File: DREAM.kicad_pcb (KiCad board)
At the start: 2 copper layers, 100 x 60 mm, 137 parts, among them J401 KLDX-0202-B, J402 EBWA-02-B, J501 Conn_ST_STDC14, J502 USB4105-GF-A, J601 1-1337535-0, J602 1-1337535-0, J603 1-1337535-0, J701 PH1-02-UA, Q401 MCU18P10Y-TP, SW501 PTS526SK15SMTR2 LFS, U401 TPS7A2030PDBVR, U501 STM32G441KBT6, U502 USBLC6-2SC6, U601 TSV912AIDR, U602 TSV912AIDR, U603 LM358LVIDR, U604 TSV912AIDR, U605 TSV912AIDR, U701 LM358LVIDR, U702 LM358LVIDR, Y501 ATS08A-E

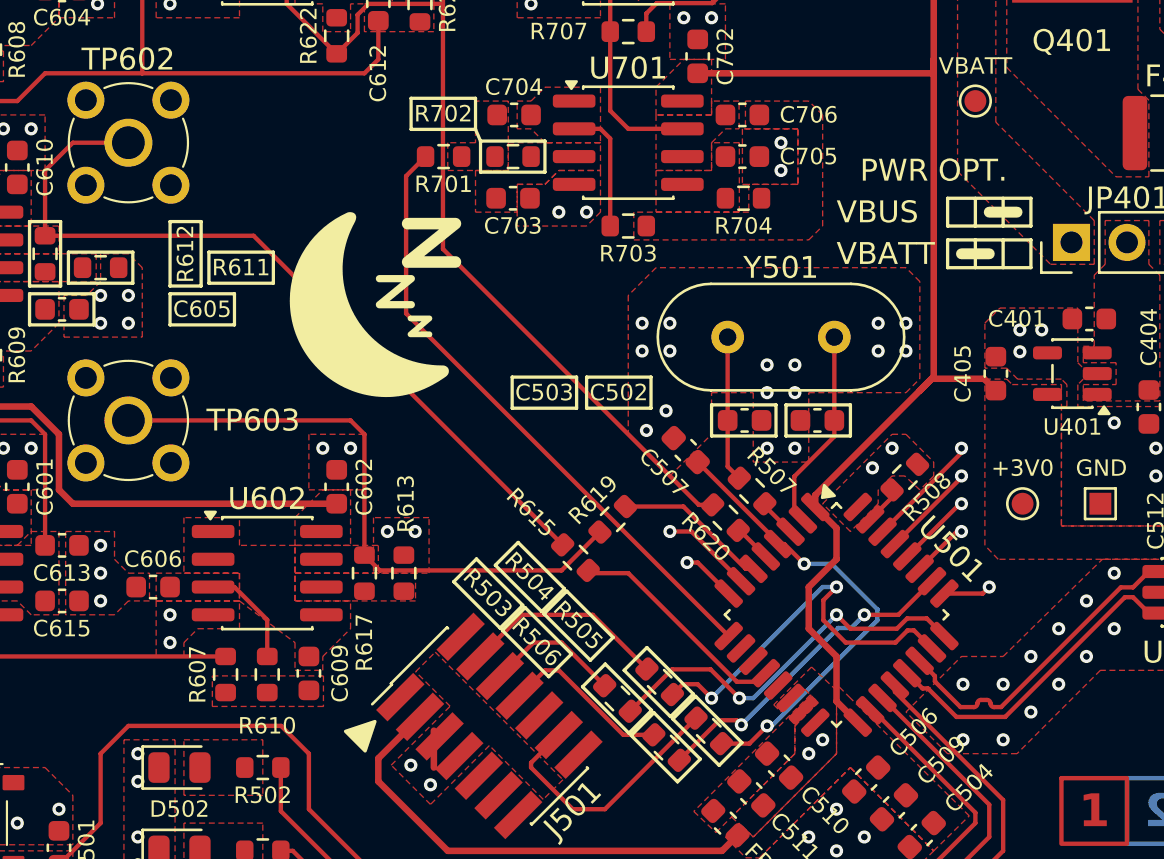
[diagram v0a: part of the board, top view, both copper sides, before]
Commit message: fix: improved crystal oscillator layout
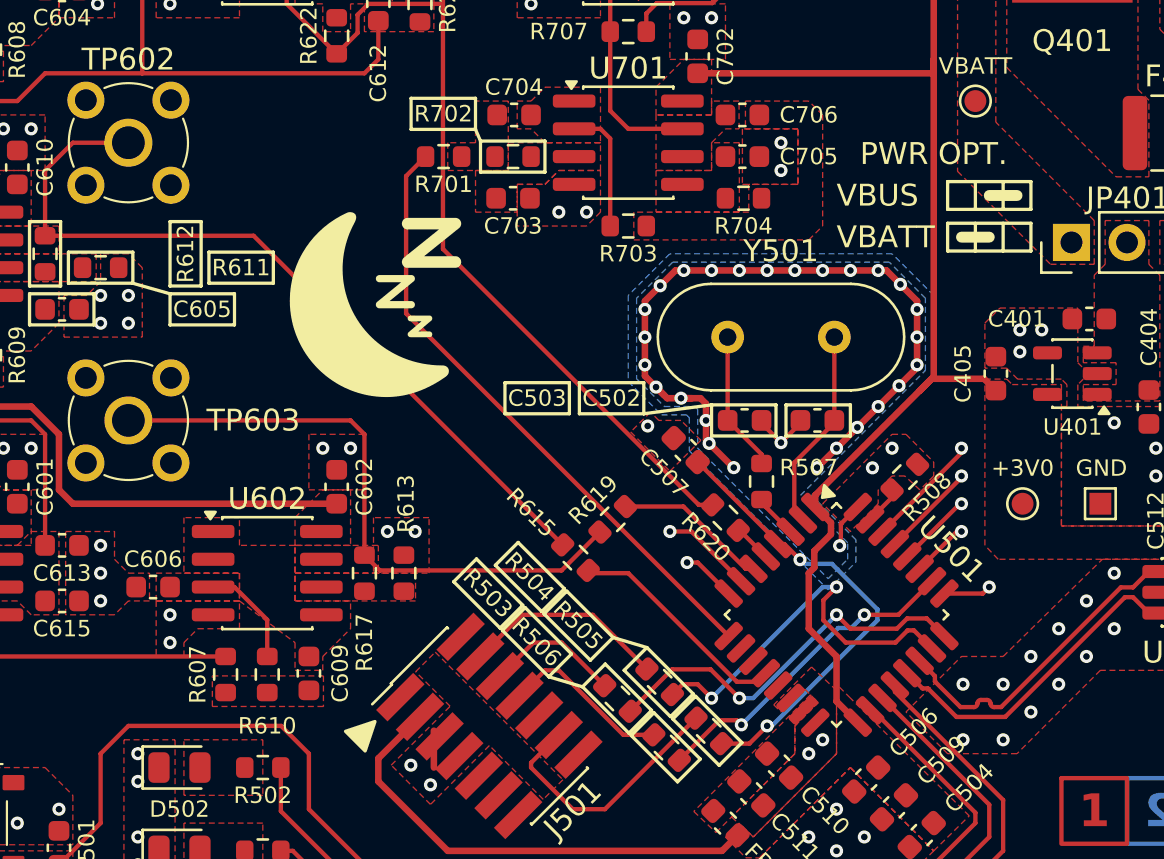
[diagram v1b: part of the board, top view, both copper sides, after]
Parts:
- moved R507 0.61 mm to (228.3, 142.4), turned to -90 degrees
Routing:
- net GND: track 2.72 -> 42.0 mm, vias 126 -> 139

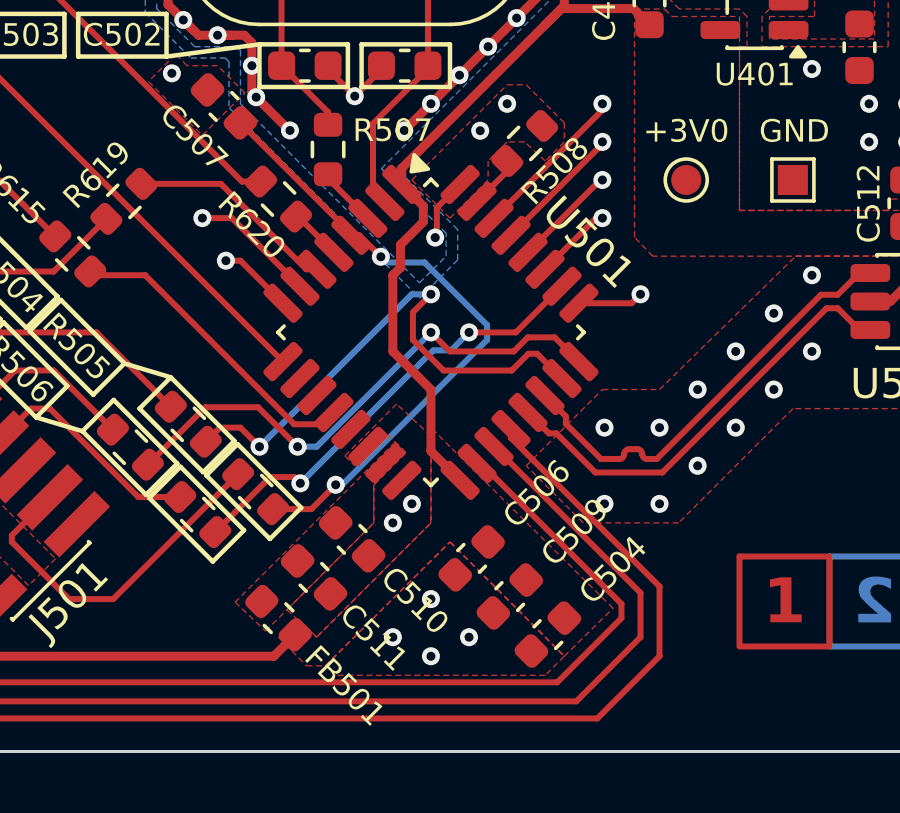
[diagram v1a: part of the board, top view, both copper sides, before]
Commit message: fix: add ground pour under uC
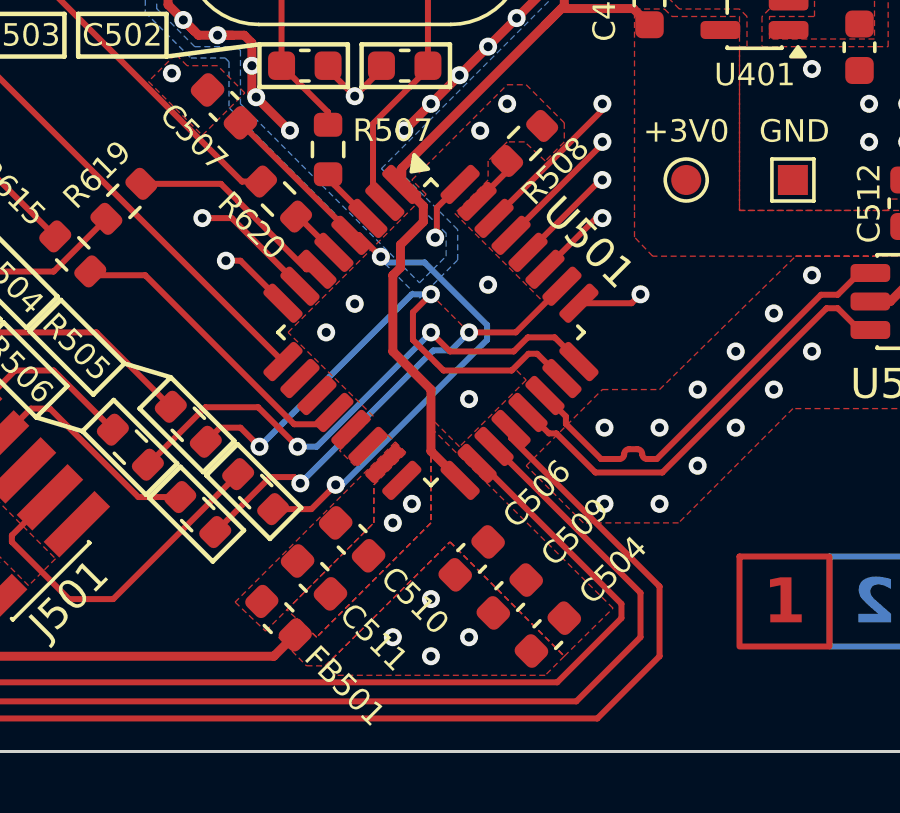
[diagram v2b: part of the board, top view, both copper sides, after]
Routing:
- net GND: vias 139 -> 143
